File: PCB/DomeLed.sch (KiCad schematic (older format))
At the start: 3 parts, among them Q24 BC817

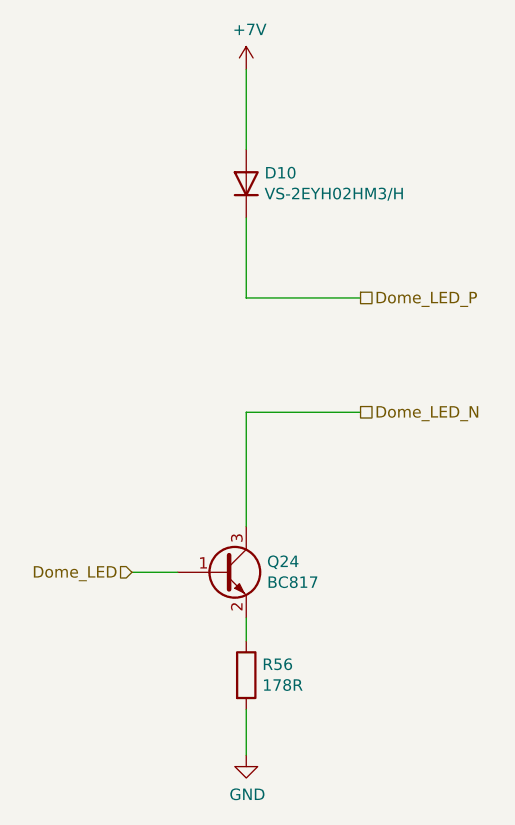
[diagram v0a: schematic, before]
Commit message: Re-annotate all components
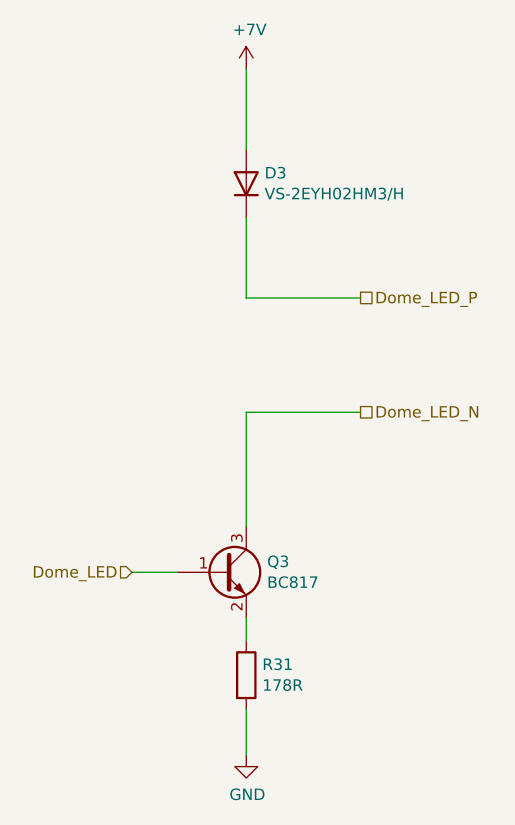
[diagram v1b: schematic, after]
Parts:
- renumbered D10 to D3, Q24 to Q3, R56 to R31
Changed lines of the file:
@@
 $Descr A4 11693 8268
 encoding utf-8
-Sheet 22 22
+Sheet 10 22
 Title "Litter Robot 3 - Dome LED control"
-Date "2021-04-03"
+Date "2021-04-05"
 Rev "A1"
 Comp "L. Sartory"
@@
 AR Path="/603F1F4D/605BE11A/60786C2B" Ref="#PWR?"  Part="1"
 AR Path="/603F1F4D/605BE15A/60786C2B" Ref="#PWR?"  Part="1"
-AR Path="/60779D3B/60786C2B" Ref="#PWR0119"  Part="1"
-F 0 "#PWR0119" H 5500 4750 50  0001 C CNN
+AR Path="/60779D3B/60786C2B" Ref="#PWR083"  Part="1"
+F 0 "#PWR083" H 5500 4750 50  0001 C CNN
 F 1 "GND" H 5505 4827 50  0000 C CNN
 F 2 "" H 5500 5000 50  0001 C CNN
@@
 AR Path="/603F1F4D/605BE11A/60786C52" Ref="Q?"  Part="1"
 AR Path="/603F1F4D/605BE15A/60786C52" Ref="Q?"  Part="1"
-AR Path="/60779D3B/60786C52" Ref="Q24"  Part="1"
-F 0 "Q24" H 5591 4246 50  0000 L CNN
+AR Path="/60779D3B/60786C52" Ref="Q3"  Part="1"
+F 0 "Q3" H 5591 4246 50  0000 L CNN
 F 1 "BC817" H 5591 4155 50  0000 L CNN
 F 2 "Package_TO_SOT_SMD:SOT-23" H 5600 4125 50  0001 L CIN
@@
 AR Path="/603F1F4D/605BE11A/60786C03" Ref="R?"  Part="1"
 AR Path="/603F1F4D/605BE15A/60786C03" Ref="R?"  Part="1"
-AR Path="/60779D3B/60786C03" Ref="R56"  Part="1"
-F 0 "R56" H 5570 4696 50  0000 L CNN
+AR Path="/60779D3B/60786C03" Ref="R31"  Part="1"
+F 0 "R31" H 5570 4696 50  0000 L CNN
 F 1 "178R" H 5570 4605 50  0000 L CNN
 F 2 "Resistor_SMD:R_0603_1608Metric" V 5430 4650 50  0001 C CNN
@@
 AR Path="/603F1F4D/605BE11A/60786C4B" Ref="#PWR?"  Part="1"
 AR Path="/603F1F4D/605BE15A/60786C4B" Ref="#PWR?"  Part="1"
-AR Path="/60779D3B/60786C4B" Ref="#PWR0118"  Part="1"
-F 0 "#PWR0118" H 5500 1850 50  0001 C CNN
+AR Path="/60779D3B/60786C4B" Ref="#PWR082"  Part="1"
+F 0 "#PWR082" H 5500 1850 50  0001 C CNN
 F 1 "+7V" H 5515 2173 50  0000 C CNN
 F 2 "" H 5500 2000 50  0001 C CNN
@@
 	5500 2650 5500 3000
 $Comp
-L Device:D D10
+L Device:D D3
 U 1 1 607AEF84
 P 5500 2500
-F 0 "D10" V 5546 2420 50  0000 R CNN
+F 0 "D3" V 5546 2420 50  0000 R CNN
 F 1 "VS-2EYH02HM3/H" V 5455 2420 50  0000 R CNN
 F 2 "Diode_SMD:D_SOD-128" H 5500 2500 50  0001 C CNN

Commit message: Add a 3D model for the SlimSMAW diodes
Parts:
- D3: footprint Diode_SMD:D_SOD-128 -> LitterRobot:Vishay_SlimSMAW
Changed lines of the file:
@@
 F 0 "D3" V 5546 2420 50  0000 R CNN
 F 1 "VS-2EYH02HM3/H" V 5455 2420 50  0000 R CNN
-F 2 "Diode_SMD:D_SOD-128" H 5500 2500 50  0001 C CNN
+F 2 "LitterRobot:Vishay_SlimSMAW" H 5500 2500 50  0001 C CNN
 F 3 "https://www.vishay.com/docs/96383/vs-2eyh02hm3.pdf" H 5500 2500 50  0001 C CNN
 F 4 "VS-2EYH02HM3/H" V 5500 2500 50  0001 C CNN "Part_number"

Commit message: Export BOM
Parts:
- R31: Part_number CR0603-FX-1780ELF -> CR0603-FX-1780ELF
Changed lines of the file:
@@
 F 2 "Resistor_SMD:R_0603_1608Metric" V 5430 4650 50  0001 C CNN
 F 3 "https://www.bourns.com/docs/product-datasheets/CRxxxxx.pdf" H 5500 4650 50  0001 C CNN
-F 4 "CR0603-FX-1780ELF" H 5500 4650 50  0001 C CNN "Part_number"
+F 4 "CR0603-FX-1780ELF" H 5500 4650 50  0001 C CNN "Part_number"
 	1    5500 4650
 	1    0    0    -1

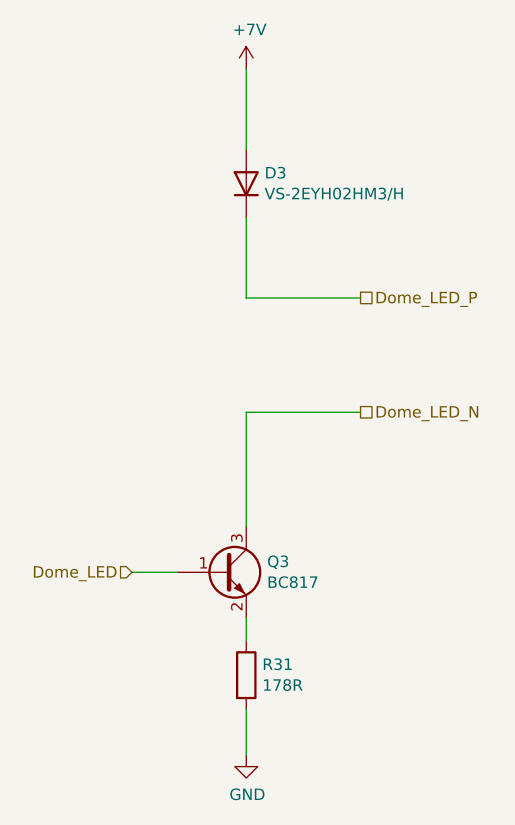
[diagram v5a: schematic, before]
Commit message: Add jumpers on the power supply outputs
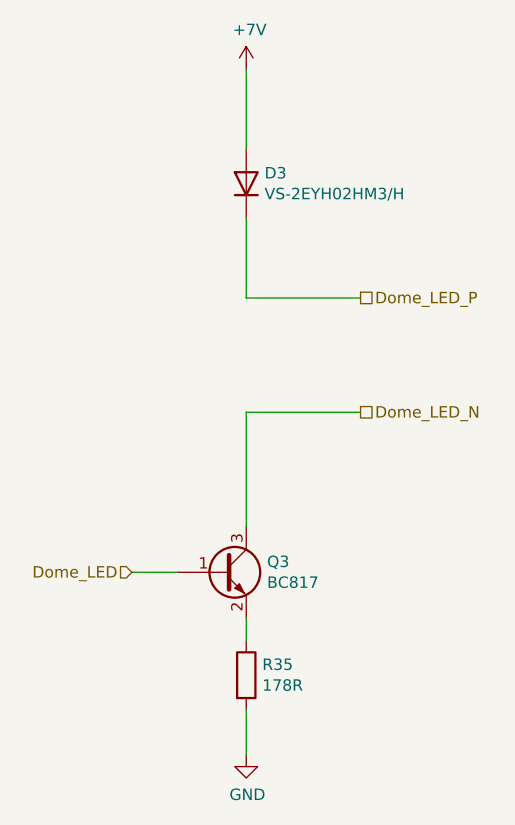
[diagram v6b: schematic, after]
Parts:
- renumbered R31 to R35
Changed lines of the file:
@@
 Sheet 11 23
 Title "Litter Robot 3 - Dome LED control"
-Date "2021-04-10"
+Date "2021-05-24"
 Rev "A1"
 Comp "L. Sartory"
@@
 AR Path="/603F1F4D/605BE11A/60786C03" Ref="R?"  Part="1"
 AR Path="/603F1F4D/605BE15A/60786C03" Ref="R?"  Part="1"
-AR Path="/60779D3B/60786C03" Ref="R31"  Part="1"
-F 0 "R31" H 5570 4696 50  0000 L CNN
+AR Path="/60779D3B/60786C03" Ref="R35"  Part="1"
+F 0 "R35" H 5570 4696 50  0000 L CNN
 F 1 "178R" H 5570 4605 50  0000 L CNN
 F 2 "Resistor_SMD:R_0603_1608Metric" V 5430 4650 50  0001 C CNN
